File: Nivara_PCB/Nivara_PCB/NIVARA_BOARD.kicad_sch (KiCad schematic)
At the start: 5 parts, among them U3 ESP32-S3-WROOM-1

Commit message: TERMINACIONES Y AJUSTES FINALES
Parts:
- added LED2: LiteOn_LTST-C19HE1WT, PCM_LED_SMD_AKL:LED_LiteOn_LTST-C19HE1WT, symbol PCM_LED_AKL:LiteOn_LTST-C19HE1WT
- added R3, R4, R5: 20, PCM_Resistor_SMD_AKL:R_0603_1608Metric, symbol EasyEDA:R_0603
- C2: value 22uF -> 2.2uF; LCSC Part (none) -> C913904; Part # (none) -> CL10A225KB8NNNC; Vol 10V -> (none)
- C3: LCSC Part (none) -> C77058; Part # (none) -> GRM188R72A104KA35D; Vol 10V -> (none)
- R6: renamed from R1; LCSC Part (none) -> C23140; Part # (none) -> 0603WAF330JT5E
- R7: renamed from R2; LCSC Part (none) -> C23140; Part # (none) -> 0603WAF330JT5E
- U5: renamed from U3; footprint RF_Module:ESP32-S3-WROOM-1 -> RF_Module:ESP32-S3-WROOM-1U; LCSC Part (none) -> C3013946; Part # (none) -> ESP32-S3-WROOM-1U-N16R8
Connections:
- net +3.3V: now also LED2.4 (A)
- net A_I_OUT/SCLK_C: now also U5.25 (GPIO48/SPICLK_N/SUBSPICLK_N_DIFF); no longer U5.26 (GPIO45)
- net A_I_OUT/SDA_C: now also U5.26 (GPIO45); no longer U5.25 (GPIO48/SPICLK_N/SUBSPICLK_N_DIFF)
- net USB_D+: now also U5.14 (GPIO20/U1CTS/ADC2_CH9/CLK_OUT1/USB_D+); no longer U5.13 (GPIO19/U1RTS/ADC2_CH8/CLK_OUT2/USB_D-)
- net USB_D-: now also U5.13 (GPIO19/U1RTS/ADC2_CH8/CLK_OUT2/USB_D-); no longer U5.14 (GPIO20/U1CTS/ADC2_CH9/CLK_OUT1/USB_D+)
- net at U5.32 (MTCK/GPIO39/CLK_OUT3/SUBSPICS1): now also R3.2
- net at U5.33 (MTDO/GPIO40/CLK_OUT2): now also R4.2
- net at U5.34 (MTDI/GPIO41/CLK_OUT1): now also R5.2
- new net: LED2.1 (R), R3.1
- new net: LED2.2 (G), R4.1
- new net: LED2.3 (B), R5.1
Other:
- moved on the sheet: R6, R7

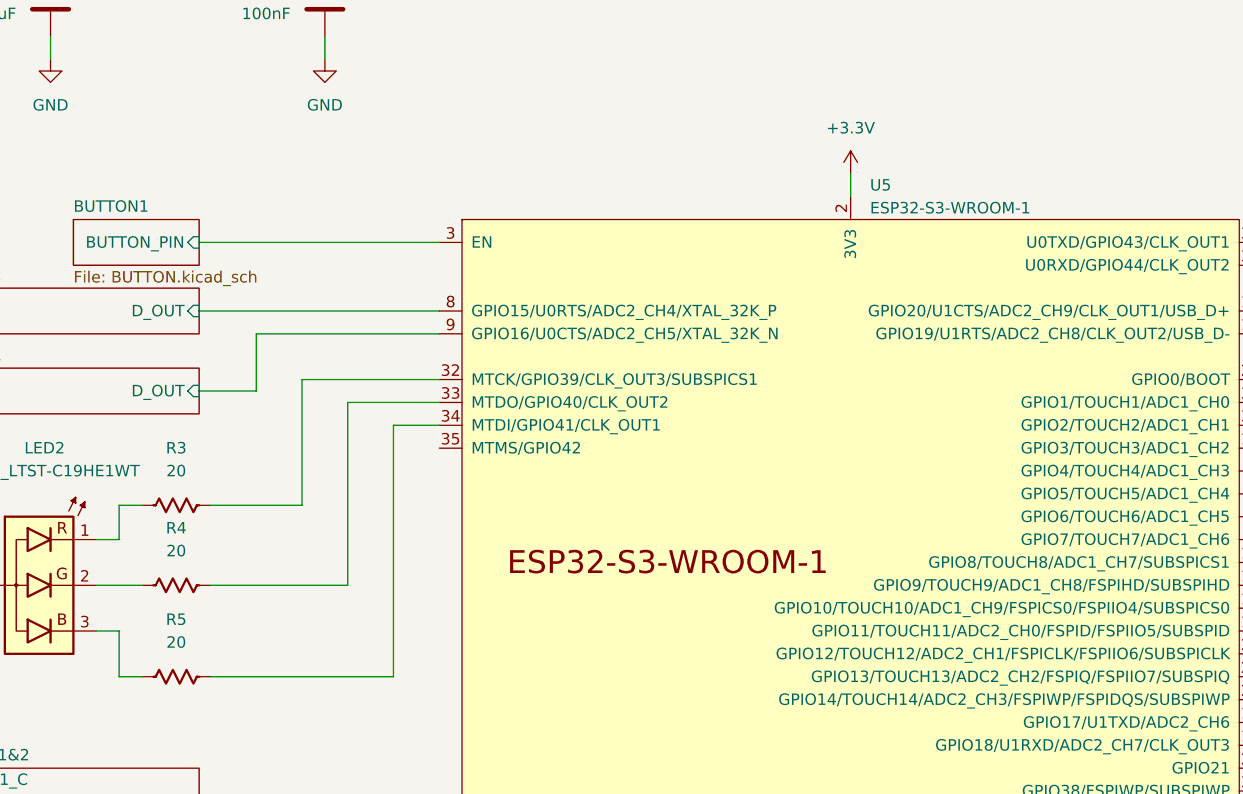
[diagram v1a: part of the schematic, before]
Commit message: Cambios en las silscreen de los componentes.
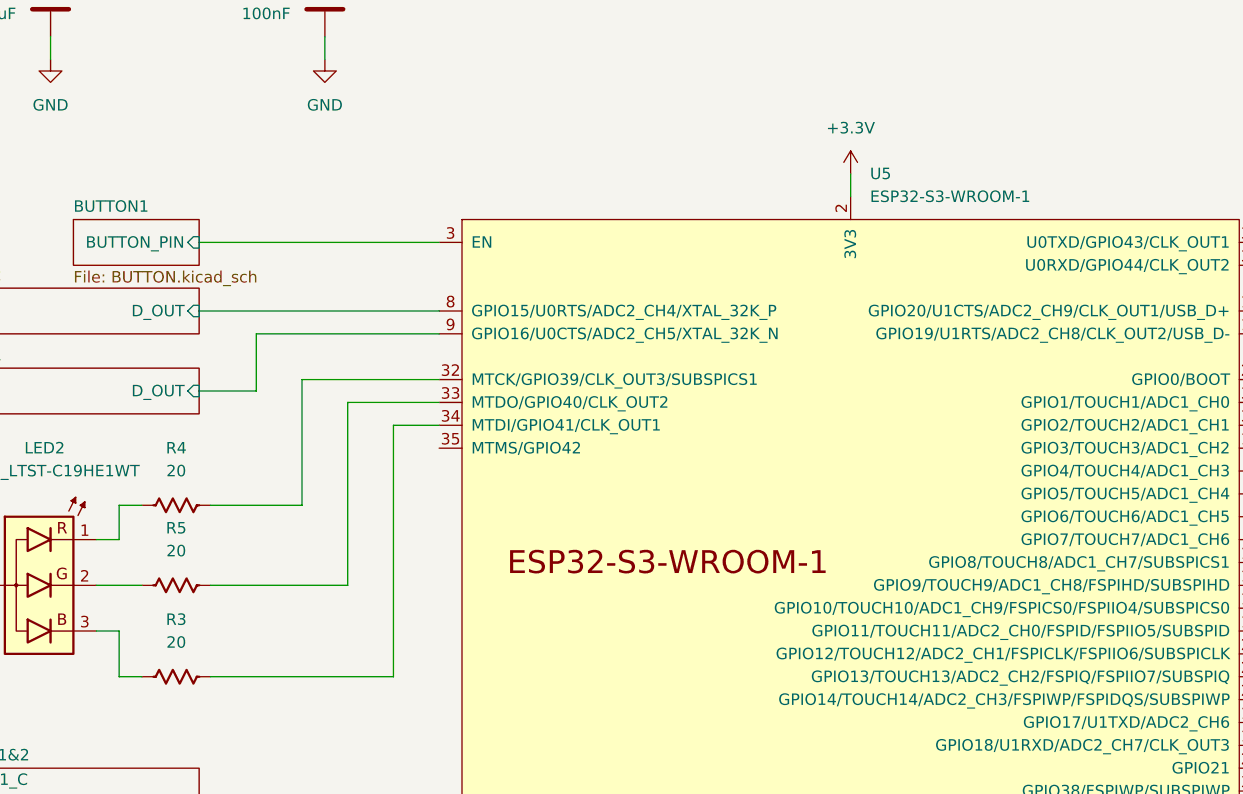
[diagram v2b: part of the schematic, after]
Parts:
- renumbered R5 to R3, R3 to R4, R4 to R5
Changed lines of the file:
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@@
 		(dnp no)
 		(fields_autoplaced yes)
-		(property "Reference" "R3"
+		(property "Reference" "R4"
 			(at 62.23 86.36 90)
 			(effects
@@
 			(project "Nivara_PCB"
 				(path "/13184db0-a71d-4054-b13a-bbf46d2b100d/4e7fa7f2-8bf5-4f9c-874d-fa1b4fd76f92"
-					(reference "R3")
+					(reference "R4")
 					(unit 1)
 				)
@@
 		(dnp no)
 		(fields_autoplaced yes)
-		(property "Reference" "#PWR021"
+		(property "Reference" "#PWR023"
 			(at 137.16 59.69 0)
 			(effects
@@
 			(project "Nivara_PCB"
 				(path "/13184db0-a71d-4054-b13a-bbf46d2b100d/4e7fa7f2-8bf5-4f9c-874d-fa1b4fd76f92"
-					(reference "#PWR021")
+					(reference "#PWR023")
 					(unit 1)
 				)
@@
 		(fields_autoplaced yes)
 		(property "Reference" "U5"
-			(at 139.3033 57.15 0)
+			(at 139.3033 55.88 0)
 			(effects
 				(font
@@
 		)
 		(property "Value" "ESP32-S3-WROOM-1"
-			(at 139.3033 59.69 0)
+			(at 139.3033 58.42 0)
 			(effects
 				(font
@@
 		(on_board yes)
 		(dnp no)
-		(property "Reference" "#PWR016"
+		(property "Reference" "#PWR018"
 			(at 33.02 97.79 0)
 			(effects
@@
 			(project "Nivara_PCB"
 				(path "/13184db0-a71d-4054-b13a-bbf46d2b100d/4e7fa7f2-8bf5-4f9c-874d-fa1b4fd76f92"
-					(reference "#PWR016")
+					(reference "#PWR018")
 					(unit 1)
 				)
@@
 		(dnp no)
 		(fields_autoplaced yes)
-		(property "Reference" "#PWR022"
+		(property "Reference" "#PWR024"
 			(at 137.16 148.59 0)
 			(effects
@@
 			(project "Nivara_PCB"
 				(path "/13184db0-a71d-4054-b13a-bbf46d2b100d/4e7fa7f2-8bf5-4f9c-874d-fa1b4fd76f92"
-					(reference "#PWR022")
+					(reference "#PWR024")
 					(unit 1)
 				)
@@
 		(on_board yes)
 		(dnp no)
-		(property "Reference" "#PWR019"
+		(property "Reference" "#PWR021"
 			(at 78.74 33.02 0)
 			(effects
@@
 			(project "Nivara_PCB"
 				(path "/13184db0-a71d-4054-b13a-bbf46d2b100d/4e7fa7f2-8bf5-4f9c-874d-fa1b4fd76f92"
-					(reference "#PWR019")
+					(reference "#PWR021")
 					(unit 1)
 				)
@@
 		(dnp no)
 		(fields_autoplaced yes)
-		(property "Reference" "#PWR020"
+		(property "Reference" "#PWR022"
 			(at 78.74 49.53 0)
 			(effects
@@
 			(project "Nivara_PCB"
 				(path "/13184db0-a71d-4054-b13a-bbf46d2b100d/4e7fa7f2-8bf5-4f9c-874d-fa1b4fd76f92"
-					(reference "#PWR020")
+					(reference "#PWR022")
 					(unit 1)
 				)
@@
 		(on_board yes)
 		(dnp no)
-		(property "Reference" "#PWR017"
+		(property "Reference" "#PWR019"
 			(at 48.26 33.02 0)
 			(effects
@@
 			(project "Nivara_PCB"
 				(path "/13184db0-a71d-4054-b13a-bbf46d2b100d/4e7fa7f2-8bf5-4f9c-874d-fa1b4fd76f92"
-					(reference "#PWR017")
+					(reference "#PWR019")
 					(unit 1)
 				)
@@
 		(dnp no)
 		(fields_autoplaced yes)
-		(property "Reference" "#PWR018"
+		(property "Reference" "#PWR020"
 			(at 48.26 49.53 0)
 			(effects
@@
 			(project ""
 				(path "/13184db0-a71d-4054-b13a-bbf46d2b100d/4e7fa7f2-8bf5-4f9c-874d-fa1b4fd76f92"
-					(reference "#PWR018")
+					(reference "#PWR020")
 					(unit 1)
 				)
@@
 		(dnp no)
 		(fields_autoplaced yes)
-		(property "Reference" "R4"
+		(property "Reference" "R5"
 			(at 62.23 95.25 90)
 			(effects
@@
 			(project "Nivara_PCB"
 				(path "/13184db0-a71d-4054-b13a-bbf46d2b100d/4e7fa7f2-8bf5-4f9c-874d-fa1b4fd76f92"
-					(reference "R4")
+					(reference "R5")
 					(unit 1)
 				)
@@
 		(dnp no)
 		(fields_autoplaced yes)
-		(property "Reference" "R5"
+		(property "Reference" "R3"
 			(at 62.23 105.41 90)
 			(effects
@@
 			(project "Nivara_PCB"
 				(path "/13184db0-a71d-4054-b13a-bbf46d2b100d/4e7fa7f2-8bf5-4f9c-874d-fa1b4fd76f92"
-					(reference "R5")
-					(unit 1)
-				)
+					(reference "R3")
+					(unit 1)
+				)
